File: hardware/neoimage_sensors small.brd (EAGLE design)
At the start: 28.3 x 23.5 mm, 27 parts, among them U1 LIS3DH, U2 OPA344, U3 ICS-40300, U4 STM32F030F4P6TR, U5 TEMT6000

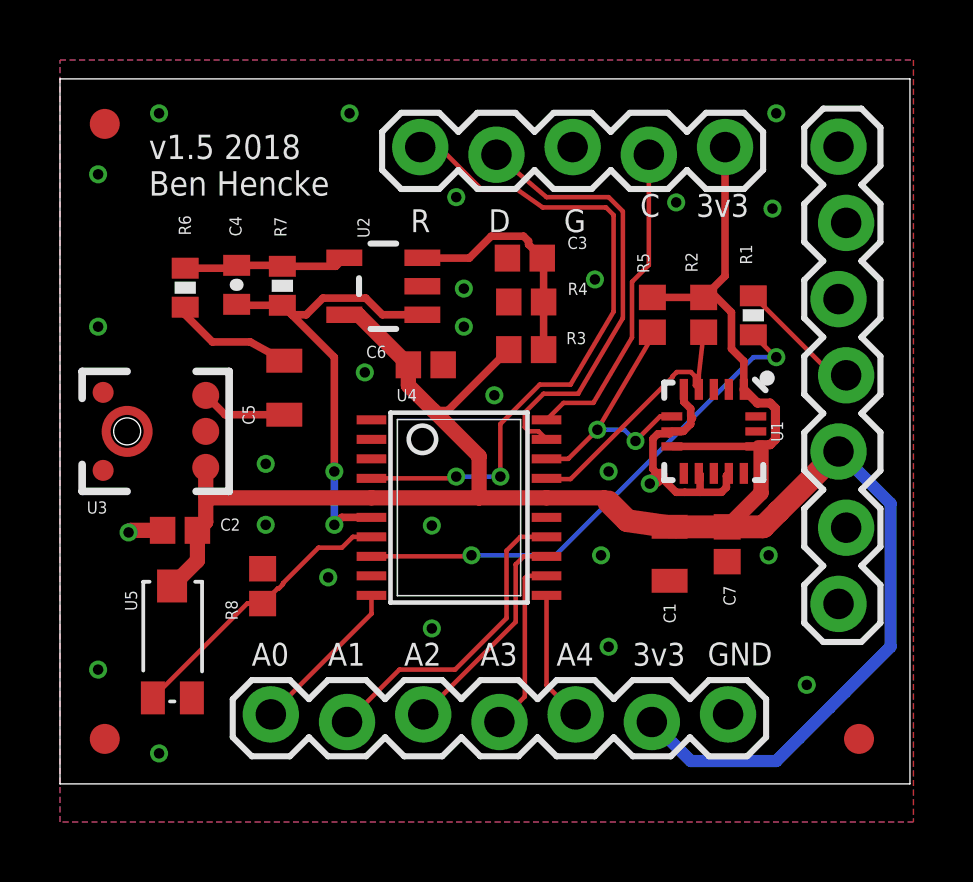
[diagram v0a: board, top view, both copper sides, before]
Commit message: v1.8 of board
switch to 0603, fix analog, labels
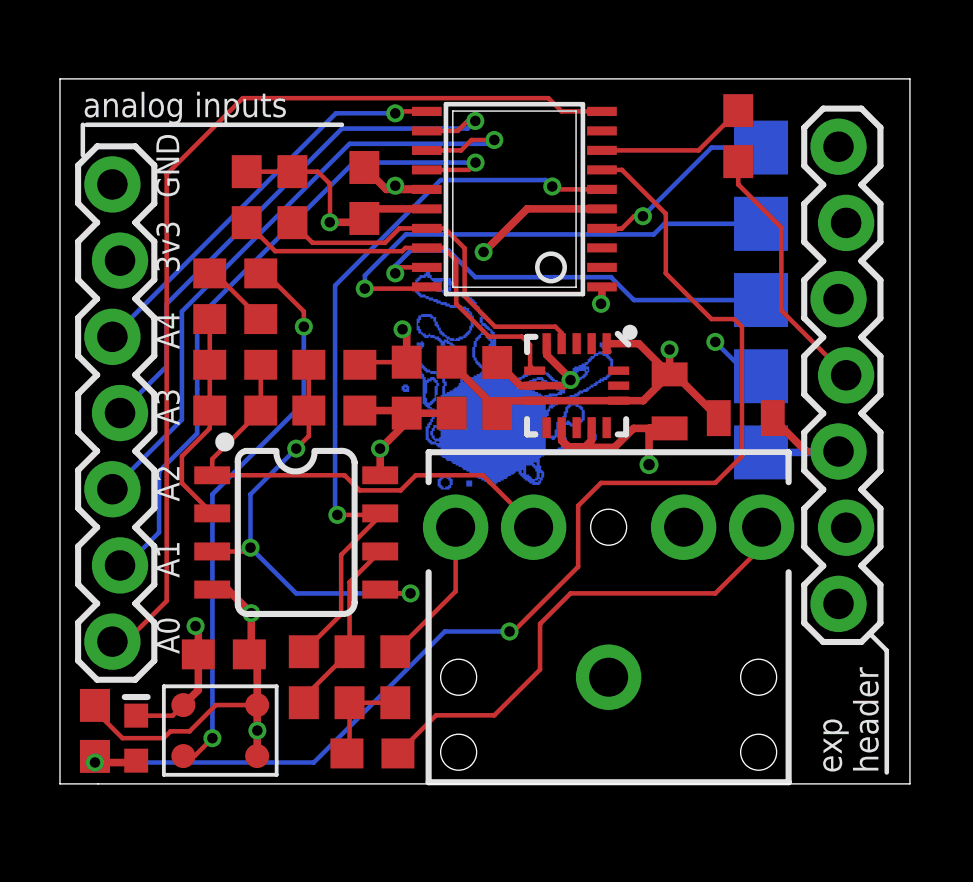
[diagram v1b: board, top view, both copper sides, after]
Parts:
- removed C3, C6: 0.1uF, SparkFun-Capacitors:0402
- removed C4: 100pF, SparkFun:0402-CAP
- removed C5: 22uF, SparkFun-Capacitors:0805
- removed FID1, FID2, FID3: FIDUCIAL, adafruit:FIDUCIAL_1MM
- removed J2: (no value), SparkFun-Connectors:1X05_LOCK
- removed R4: 10k, SparkFun-Resistors:0402
- removed R6: 10k, SparkFun:0402-RES
- removed R7: 100K, SparkFun:0402-RES
- removed U$1: (no value), bens:EM-LOGO4
- removed U3: ICS-40300, SparkFun:ADMP401
- removed U5: TEMT6000, SparkFun:TEMT6000-SEN
- added 3V, C, D, G, N: TPSQTP18SQ, testpad:TP18SQ
- added C10, C13: 4.7uF, SparkFun-Capacitors:0603
- added C12: 1.0uF, SparkFun-Capacitors:0603
- added C8: 0.1uF, SparkFun-Capacitors:0603
- added C9: 100pF, SparkFun-Capacitors:0603
- added J8: AUDIO_JACK_3.5MM, SparkFun-Connectors:AUDIO-JACK-KIT
- added L1: 3.3µH/±20%/450mA, SparkFun-Coils:0805
- added R13, R14, R17, R18, R19: 10k, SparkFun-Resistors:0603
- added R15: 4.7k, SparkFun-Resistors:0603
- added R16: 100k, SparkFun-Resistors:0603
- added U$3: MICROPHONE-MEMS, bens:MICROPHONE-MEMS-3X3.75
- added U$4: (no value), Electro_Mage_pcb4_pixel_6:ELECTRO_MAGE_PCB4_PIXEL_2#PNG
- added U6: LMV358, SparkFun-IC-Amplifiers:SO08
- C2, C7: device SparkFun-Capacitors:0402 -> SparkFun-Capacitors:0603
- R1: value 1.5K -> 1.5k; device SparkFun:0402-RES -> SparkFun-Resistors:0603
- R2, R5, R8: device SparkFun-Resistors:0402 -> SparkFun-Resistors:0603
- R3: value 10k -> 33; device SparkFun-Resistors:0402 -> SparkFun-Resistors:0603
- U2: value OPA344 -> LIGHT_SENSORALS; device SparkFun:SOT23-5 -> SparkFun-Sensors:ALS-PT19
- moved U2 17.2 mm to (2.54, 1.52), turned to 270 degrees
- moved C7 16.8 mm to (10.1, 19.7), turned to 90 degrees
- moved R2 14.3 mm to (7.75, 19.6)
- moved R5 14.1 mm to (6.22, 19.6)
- moved C2 11.6 mm to (14.6, 13.2), turned to 90 degrees
- moved U4 10.4 mm to (15.1, 19.5), turned to 90 degrees
- moved R8 7.38 mm to (1.17, 1.77)
- moved R1 5.99 mm to (22.6, 21.6), turned to 90 degrees
- moved J3 5.75 mm to (1.87, 4.74), turned to 90 degrees
- moved C1 5.08 mm to (20.3, 12.8)
- moved U1 4.82 mm to (17.2, 13.3)
- moved R3 2.79 mm to (13.1, 13.2), turned to 270 degrees
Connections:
- removed net N$3: C4.1, R6.1, R7.2, U2.4
- removed net N$6: C5.2, R6.2
- removed net N$7: C3.1, R3.1, R4.2, U2.3
- removed net PA0: C4.2, R7.1, U2.1, U4.6
- new net AUDIO: R17.2, U4.6, U6.7
- new net MICOUT: C9.2, J8.RSH, R16.1, U6.1
- new net N$1: U4.3
- new net N$21: C10.1, U$3.4
- new net N$22: C9.1, R15.1, R16.2, U6.2
- new net N$23: C10.2, R15.2
- new net N$24: R13.1, R14.2, U6.3, U6.5
- new net N$25: C12.1, R18.1, R19.1
- new net N$26: C12.2, R17.1, U6.6
- new net N$27: J8.TIP, R19.2
- new net N$28: J8.RING, R18.2
- new net VDDA: C13.1, C8.1, R13.2, R3.2, U$3.1, U2.C, U4.5, U6.8
- new net VIN: 3V.TP, J1.3, L1.2
- net +3V3: now also L1.1, R3.1; no longer C6.1, J1.3, J2.5, R3.2, U2.5, U3.5, U4.5, U5.COLLECTOR
- net GND: now also C13.2, C8.2, G.TP, J8.SLEEVE, R14.1, U$3.2, U$3.3, U6.4; no longer C3.2, C6.2, J2.3, R4.1, U2.2, U3.2, U3.4, U3.6
- net N$2: now also U4.2; no longer C5.1, U3.1
- net NRST: now also N.TP; no longer J2.1
- net PA1: now also U2.E; no longer U5.EMITTER
- net PA13: now also D.TP; no longer J2.2
- net PA14: now also C.TP; no longer J2.4
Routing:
- net +3V3: track 75.8 -> 21.9 mm, vias 0 -> 2
- net PA1: track 9.53 -> 40.9 mm, vias 0 -> 2
- net PA4: track 5.36 -> 32.3 mm
- net GND: track 9.34 -> 35.4 mm, vias 27 -> 8
- net AUDIO: track 0.00 -> 25.3 mm, vias 0 -> 2
- net N$21: track 0.00 -> 18.7 mm, vias 0 -> 2
- net VDDA: track 0.00 -> 17.9 mm, vias 0 -> 3
- net N$27: track 0.00 -> 16.5 mm
- net MICOUT: track 0.00 -> 16.2 mm
- net PA0: track 16.2 -> 0.00 mm, vias 2 -> 0
- net NRST: track 22.3 -> 6.43 mm, vias 2 -> 1
- net N$24: track 0.00 -> 15.3 mm, vias 0 -> 3
- net PA7: track 7.41 -> 22.1 mm, vias 0 -> 1
- net PA6: track 5.90 -> 18.8 mm, vias 0 -> 1
- net TX: track 17.3 -> 5.09 mm, vias 2 -> 0
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- added copper zone on layer 15, net +3V3
- added copper zone on layer 2, net GND
- added copper zone on layer 15, net VDDA
- removed copper zone on layer 1, net GND
- removed copper zone on layer 16, net GND
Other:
- outline, holes or cut-outs redrawn
- board text added: "Pixelblaze Sensor Expansion"
- board text added: "analog inputs"
- board text added: "exp header"
- board text added: "v1.8 2019 Ben Hencke"
- board text removed: "C"
- board text removed: "D"
- board text removed: "G"
- board text removed: "R"
- board text removed: "RX"
- board text removed: "v1.5 2018 Ben Hencke"
